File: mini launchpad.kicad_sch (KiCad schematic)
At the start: 75 parts, among them J1 USB_A, P1 USB_C_Plug_USB2.0, U1 MCP23017_ML, U2 MCP23017_ML, U3 MCP23017_ML, U4 MCP23017_ML, U5 CP2615-xx-xM, U6 TMUX1574PW, U7 CH334R

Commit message: pcb update
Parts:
- removed A2: RaspberryPi_Pico, Module:RaspberryPi_Pico_Common_THT, symbol MCU_Module:RaspberryPi_Pico
- removed J1: USB_A, Connector_USB:USB_A_Connfly_DS1095, symbol Connector:USB_A
- added C1, C2: 10µF, Capacitor_SMD:C_0201_0603Metric, symbol Device:C
- added C10, C11, C12, C13, C14, C4, C5, C7, C8, C9: 100nF, Capacitor_SMD:C_0201_0603Metric, symbol Device:C
- added C15, C16: 22pF, Capacitor_SMD:C_0402_1005Metric, symbol Device:C_Small
- added C3, C6: 1µF, Capacitor_SMD:C_0201_0603Metric, symbol Device:C
- added JP1: Jumper_2_Open, Jumper:Jumper_Harwin_S1621_P10.9mm, symbol Jumper:Jumper_2_Open
- added R2, R3: 27, Resistor_SMD:R_0402_1005Metric, symbol Device:R
- added R4: 10K, Resistor_SMD:R_0402_1005Metric, symbol Device:R
- added R5: 1K, Resistor_SMD:R_0402_1005Metric, symbol Device:R
- added R7: 1k, Resistor_SMD:R_0402_1005Metric, symbol Device:R_Small
- added SW65: SW_DPDT_x2, Button_Switch_THT:SW_E-Switch_EG2219_DPDT_Angled, symbol Switch:SW_DPDT_x2
- added U10: W25Q128JVS, Package_SO:SOIC-8_5.3x5.3mm_P1.27mm, symbol Memory_Flash:W25Q128JVS
- added U8: RP2040, Package_DFN_QFN:QFN-56-1EP_7x7mm_P0.4mm_EP3.2x3.2mm, symbol MCU_RaspberryPi:RP2040
- added U9: NCP1117-3.3_TO252, Package_TO_SOT_SMD:TO-252-2, symbol Regulator_Linear:NCP1117-3.3_TO252
- added Y1: 12MHz, Crystal:Crystal_SMD_3225-4Pin_3.2x2.5mm, symbol Device:Crystal_GND24_Small
- R1: value 5100 -> 5.1K
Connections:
- net +3V3: now also C10.2, C11.2, C12.1, C13.1, C14.2, C2.2, C6.1, C7.2, C8.2, C9.2, R4.1, U10.8 (VCC), U8.1 (IOVDD), U8.10 (IOVDD), U8.22 (IOVDD), U8.33 (IOVDD), U8.42 (IOVDD), U8.43 (ADC_AVDD), U8.44 (VREG_IN), U8.48 (USB_VDD), U8.49 (IOVDD), U9.2 (VO)
- net GND: now also C1.1, C10.1, C11.1, C12.2, C13.2, C14.1, C15.1, C16.1, C2.1, C3.2, C4.2, C5.2, C6.2, C7.1, C8.1, C9.1, JP1.2 (B), U10.4 (GND), U8.57 (GND), U9.1 (GND), Y1.2, Y1.4
- net INT1: now also U8.2 (GPIO0)
- net INT2: now also U8.3 (GPIO1)
- net INT3: now also U8.4 (GPIO2)
- net INT4: now also U8.5 (GPIO3)
- net PI_I²S: now also U8.37 (GPIO25)
- net SCK: now also U8.7 (GPIO5)
- net SDA: now also U8.6 (GPIO4)
- net VBUS: now also C1.2, SW65.1 (A), U9.3 (VI); no longer P1.A4 (VBUS), P1.A9 (VBUS), P1.B4 (VBUS), P1.B9 (VBUS)
- net D-1: now reaches U7.7 (DM1-)
- net D-1: now also R3.2
- net D+1: now reaches U7.8 (DP1+)
- net D+1: now also R2.1
- net PI_BLCK: now reaches U6.10 (S3B)
- net PI_BLCK: now also U8.38 (GPIO26_ADC0)
- net PI_LRCLK: now reaches U6.13 (S4B)
- net PI_LRCLK: now also U8.39 (GPIO27_ADC1)
- net PI_DIN: now reaches U6.6 (S2B)
- net PI_DIN: now also U8.40 (GPIO28_ADC2)
- new net: R4.2, R5.1, U10.1 (~{CS}), U8.56 (QSPI_SS)
- new net: U10.2 (DO/IO_{1}), U8.55 (QSPI_SD1)
- new net: U10.3 (~{WP}/IO_{2}), U8.54 (QSPI_SD2)
- new net: U10.5 (DI/IO_{0}), U8.53 (QSPI_SD0)
- new net: U10.6 (CLK), U8.52 (QSPI_SCLK)
- new net: U10.7 (~{HOLD}/~{RESET}/IO_{3}), U8.51 (QSPI_SD3)
- new net: R3.1, U8.46 (USB_DM)
- new net: C15.2, U8.20 (XIN), Y1.3
- new net: R7.2, U8.21 (XOUT)
- new net: R2.2, U8.47 (USB_DP)
- new net: P1.A4 (VBUS), P1.A9 (VBUS), P1.B4 (VBUS), P1.B9 (VBUS), SW65.2 (B)
- new net: JP1.1 (A), R5.2
- new net +1V1: C3.1, C4.1, C5.1, U8.23 (DVDD), U8.45 (VREG_VOUT), U8.50 (DVDD)
- new net XTAL_O: C16.2, R7.1, Y1.1
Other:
- note added: "P43"
- note added: "P45"
- note added: "USB input"
- note added: "USB to I²S and I²S switching"
- note added: "rp2040"
- note added: "voltage regulator"
- moved on the sheet: P1, R1, U5, U6, U7

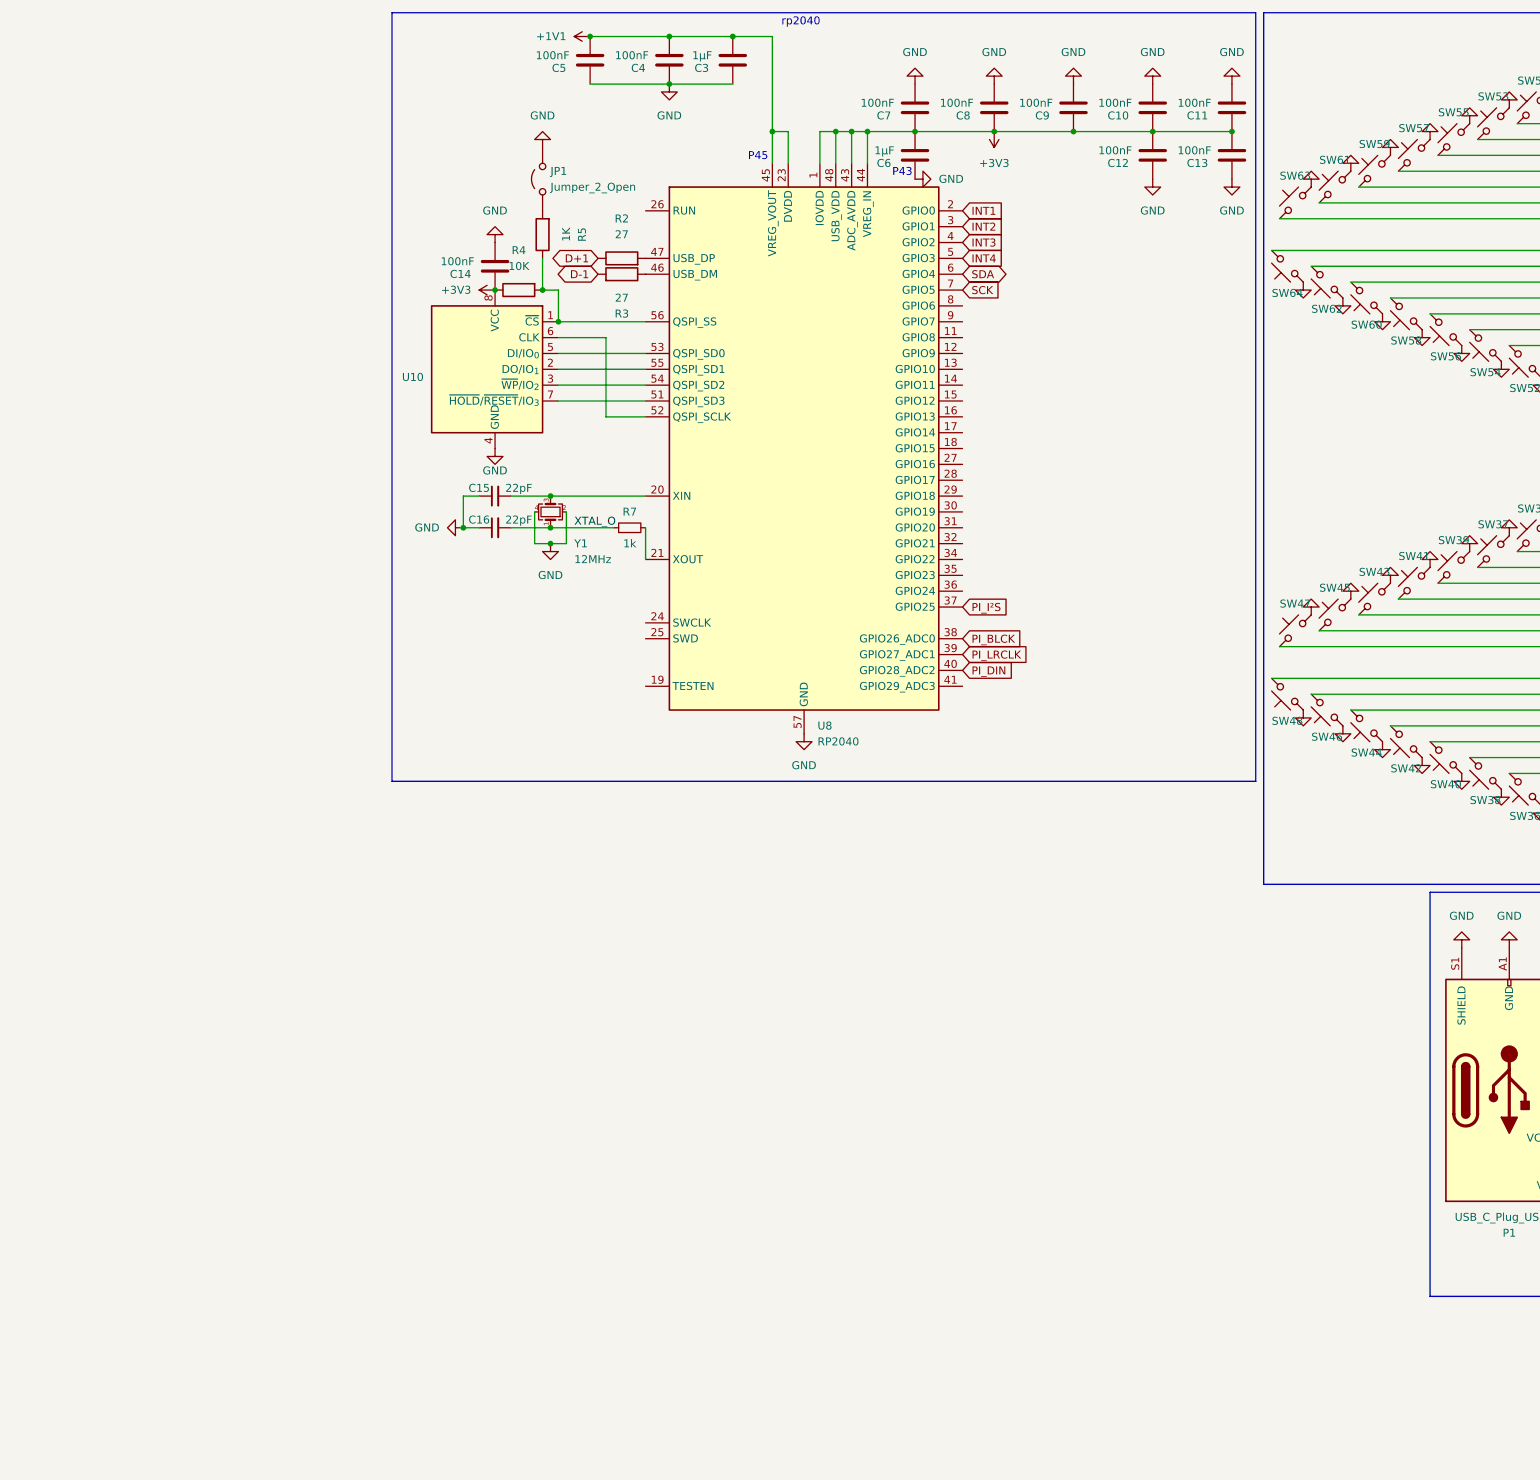
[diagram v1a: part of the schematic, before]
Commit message: schematic update
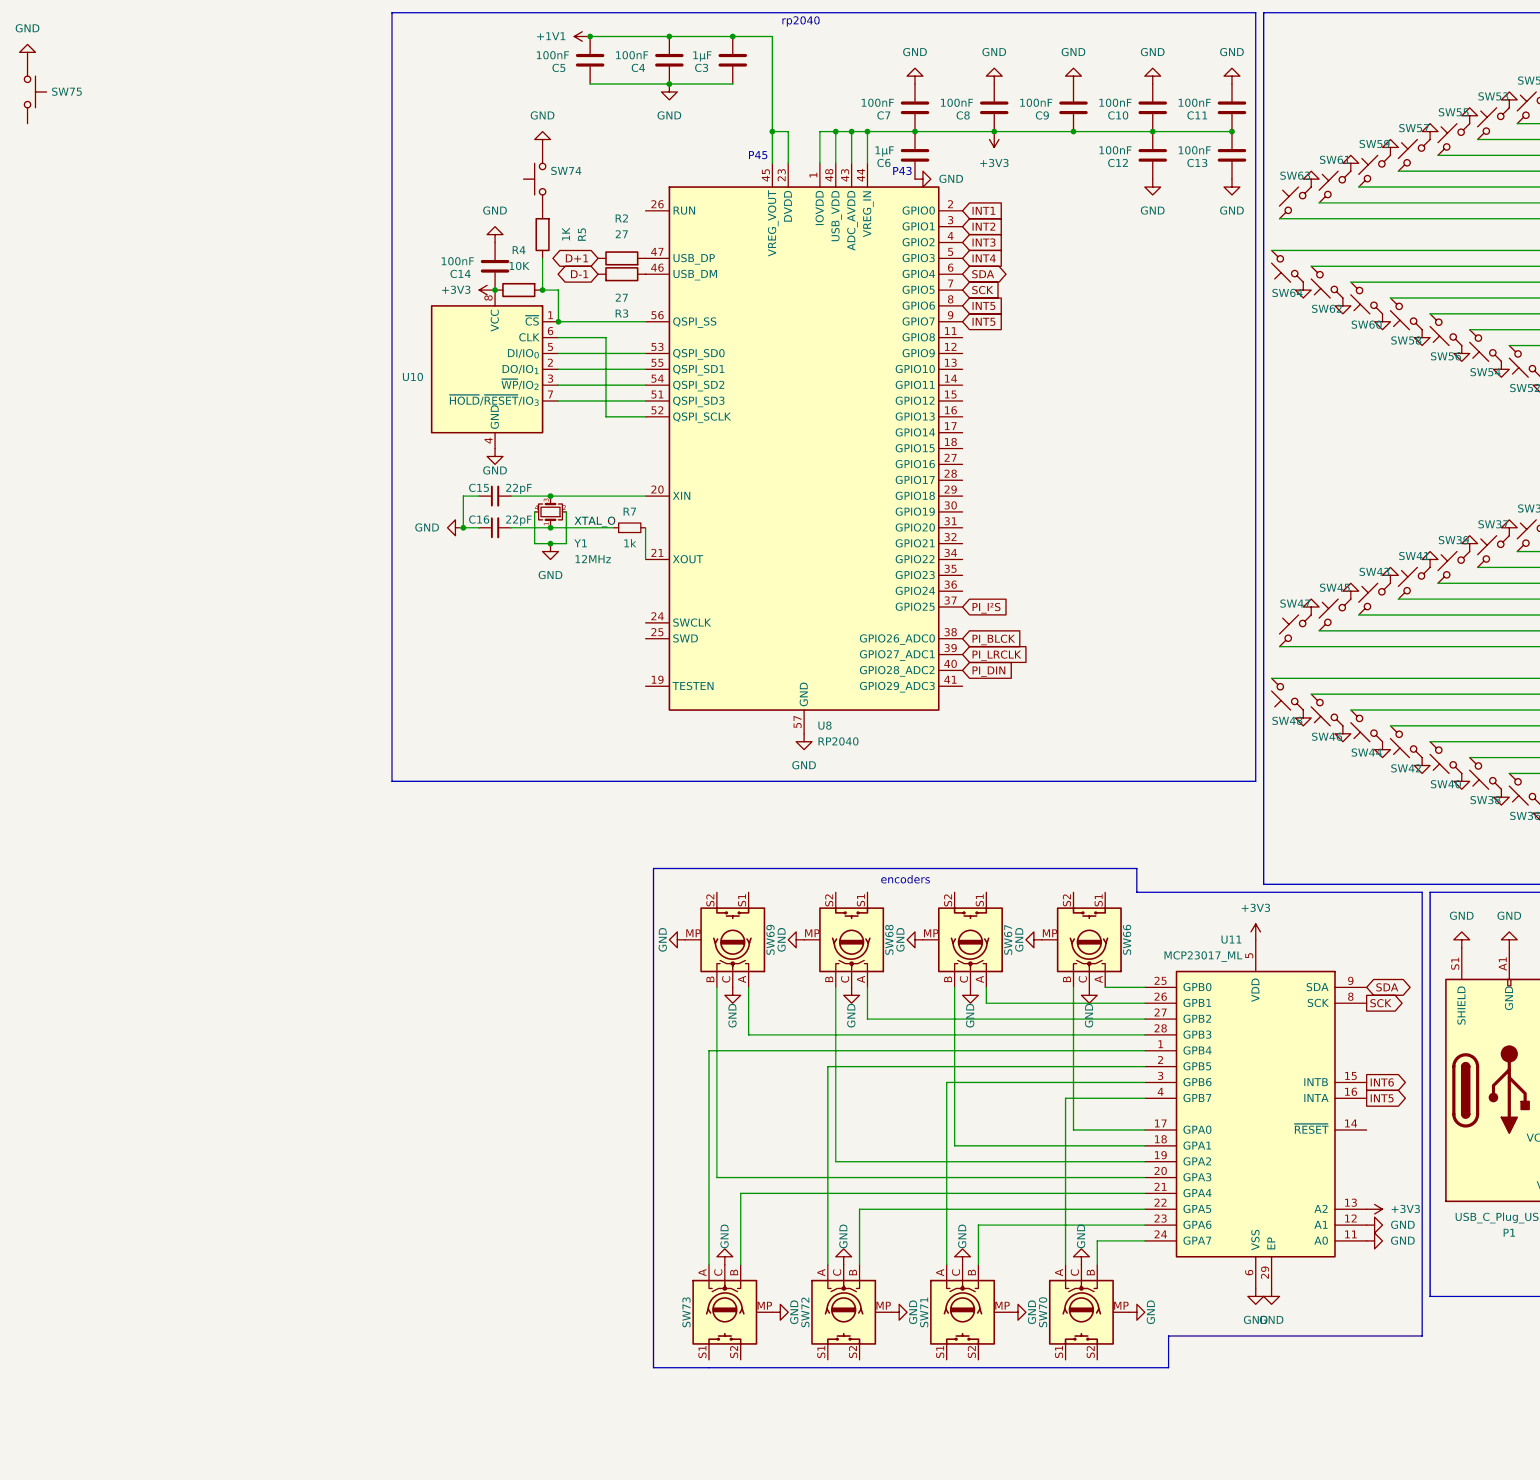
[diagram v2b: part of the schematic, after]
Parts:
- removed JP1: Jumper_2_Open, Jumper:Jumper_Harwin_S1621_P10.9mm, symbol Jumper:Jumper_2_Open
- added SW66, SW67, SW68, SW69, SW70, SW71, SW72, SW73: RotaryEncoder_Switch_MP, Rotary_Encoder:RotaryEncoder_Alps_EC11E-Switch_Vertical_H20mm_MountingHoles, symbol Device:RotaryEncoder_Switch_MP
- added SW74, SW75: SW_Push, symbol Switch:SW_Push
- added U11: MCP23017_ML, Package_DFN_QFN:QFN-28-1EP_6x6mm_P0.65mm_EP4.25x4.25mm, symbol Interface_Expansion:MCP23017_ML
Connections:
- net +3V3: now also U11.13 (A2), U11.5 (VDD)
- net GND: now also SW66.C, SW66.MP, SW67.C, SW67.MP, SW68.C, SW68.MP, SW69.C, SW69.MP, SW70.C, SW70.MP, SW71.C, SW71.MP, SW72.C, SW72.MP, SW73.C, SW73.MP, SW74.2, SW75.1, U11.11 (A0), U11.12 (A1), U11.29 (EP), U11.6 (VSS)
- net SCK: now also U11.8 (SCK)
- net SDA: now also U11.9 (SDA)
- net INT5: now reaches U8.8 (GPIO6)
- net INT5: now also U8.9 (GPIO7), U11.16 (INTA)
- net at R5.2: now also SW74.1
- new net: SW69.A, U11.28 (GPB3)
- new net: SW69.B, U11.20 (GPA3)
- new net: SW70.A, U11.4 (GPB7)
- new net: SW70.B, U11.24 (GPA7)
- new net: SW73.A, U11.1 (GPB4)
- new net: SW73.B, U11.21 (GPA4)
- new net: SW71.A, U11.3 (GPB6)
- new net: SW71.B, U11.23 (GPA6)
- new net: SW68.A, U11.27 (GPB2)
- new net: SW68.B, U11.19 (GPA2)
- new net: SW66.B, U11.17 (GPA0)
- new net: SW67.B, U11.18 (GPA1)
- new net: SW72.A, U11.2 (GPB5)
- new net: SW72.B, U11.22 (GPA5)
- new net: SW66.A, U11.25 (GPB0)
- new net: SW67.A, U11.26 (GPB1)
- new net INT6: U11.15 (INTB)
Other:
- note added: "encoders"

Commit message: pcb update
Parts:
- added D1, D2: LED, LED_SMD:LED_1206_3216Metric, symbol Device:LED
- added D3: GREEN_LED, LED_SMD:LED_1206_3216Metric, symbol Device:LED
- added R6, R8, R9: 220, Resistor_SMD:R_0402_1005Metric, symbol Device:R
- added SW76, SW77, SW78, SW79, SW80, SW81, SW82: SW_Push, Button_Switch_Keyboard:SW_Cherry_MX_1.00u_PCB, symbol Switch:SW_Push
- added SW84: RotaryEncoder_Switch_MP, Rotary_Encoder:RotaryEncoder_Alps_EC11E-Switch_Vertical_H20mm_MountingHoles, symbol Device:RotaryEncoder_Switch_MP
- SW74, SW75: footprint (none) -> Button_Switch_Keyboard:SW_Cherry_MX_1.00u_PCB
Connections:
- net GND: now also D1.1 (K), D2.1 (K), D3.1 (K), SW76.1, SW77.1, SW78.1, SW79.1, SW80.1, SW81.1, SW82.1, SW84.C, SW84.MP
- new net: D2.2 (A), R8.2
- new net: D1.2 (A), R6.2
- new net: D3.2 (A), R9.2

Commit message: pcb update
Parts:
- removed SW82: SW_Push, Button_Switch_Keyboard:SW_Cherry_MX_1.00u_PCB, symbol Switch:SW_Push
- removed SW84: RotaryEncoder_Switch_MP, Rotary_Encoder:RotaryEncoder_Alps_EC11E-Switch_Vertical_H20mm_MountingHoles, symbol Device:RotaryEncoder_Switch_MP
- added C17, C18, C21, C22: 10µF, Capacitor_SMD:C_0201_0603Metric, symbol Device:C
- added C19, C24: 250µF, Capacitor_SMD:C_0201_0603Metric, symbol Device:C
- added C20, C23: 0.05µF, Capacitor_SMD:C_0201_0603Metric, symbol Device:C
- added R10, R13: 10, Resistor_SMD:R_0402_1005Metric, symbol Device:R
- added R11, R12: 10K, Resistor_SMD:R_0402_1005Metric, symbol Device:R
- added R14, R15: 100, Resistor_SMD:R_0402_1005Metric, symbol Device:R
- added RV2: R_Potentiometer_Dual, Potentiometer_THT:Potentiometer_Alpha_RD902F-40-00D_Dual_Vertical, symbol Device:R_Potentiometer_Dual
- added SW83: SW_Push, Button_Switch_Keyboard:SW_Cherry_MX_1.00u_PCB, symbol Switch:SW_Push
- added U12, U13: LM386, Package_DIP:DIP-8_W7.62mm_Socket, symbol Amplifier_Audio:LM386
- D3: value GREEN_LED -> LED
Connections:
- net GND: now also C18.1, C22.1, R10.2, R11.1, R12.1, R13.2, SW83.1, U12.2 (-), U12.4 (GND), U13.2 (-), U13.4 (GND)
- net VBUS: now also U12.6 (V+), U13.6 (V+)
- net GPIO20: now reaches SW79.2
- net GPIO20: now also U8.31 (GPIO20)
- net GPIO16: now reaches R6.1
- net GPIO16: now also U8.27 (GPIO16)
- net GPIO18: now reaches SW80.2
- net GPIO18: now also U8.29 (GPIO18)
- net GPIO14: now reaches R9.1
- net GPIO14: now also U8.17 (GPIO14)
- net GPIO24: now reaches SW75.2
- net GPIO24: now also U8.36 (GPIO24)
- net GPIO21: now reaches SW78.2
- net GPIO21: now also U8.32 (GPIO21)
- net GPIO15: now reaches U8.18 (GPIO15)
- net GPIO15: now also R8.1
- net GPIO17: now reaches U8.28 (GPIO17)
- net GPIO17: now also SW81.2
- net GPIO19: now reaches U8.30 (GPIO19)
- net GPIO19: now also SW83.2
- net GPIO22: now reaches U8.34 (GPIO22)
- net GPIO22: now also SW77.2
- net GPIO23: now reaches U8.35 (GPIO23)
- net GPIO23: now also SW76.2
- new net: C17.1, U12.1 (GAIN)
- new net: C19.1, C20.1, U12.5
- new net: C18.2, U12.7 (BYPASS)
- new net: RV2.2, U12.8 (GAIN)
- new net: C22.2, U13.7 (BYPASS)
- new net: C23.1, C24.1, U13.5
- new net: C24.2, R15.2
- new net: C23.2, R13.1
- new net: C19.2, R14.2
- new net: C20.2, R10.1
- new net: C17.2, RV2.1
- new net: C21.1, U13.1 (GAIN)
- new net: RV2.5, U13.8 (GAIN)
- new net: C21.2, RV2.4
- new net lineL: R11.2, U12.3 (+)
- new net lineR: R12.2, U13.3 (+)
- new net outL: R14.1
- new net outR: R15.1
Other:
- note added: "amp"
- note added: "control"
- moved on the sheet: D1, D2, D3, R6, R8, R9, SW80, SW81

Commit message: pcb update
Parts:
- added J1: Conn_01x08_Socket, Connector_PinHeader_2.54mm:PinHeader_1x08_P2.54mm_Vertical, symbol Connector:Conn_01x08_Socket
- added J2: Conn_01x06_Socket, Connector_PinHeader_2.54mm:PinHeader_1x06_P2.54mm_Vertical, symbol Connector:Conn_01x06_Socket
- added Q1: AO3401A, Package_TO_SOT_SMD:SOT-23, symbol Transistor_FET:AO3401A
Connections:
- net +3V3: now also Q1.3 (D)
- net GND: now also J1.2 (Pin_2), J1.7 (Pin_7)
- net lineL: now also J1.6 (Pin_6)
- net lineR: now also J1.8 (Pin_8)
- net GPIO13: now reaches U8.16 (GPIO13)
- net GPIO13: now also Q1.1 (G)
- net LRCLK: now reaches U6.12 (D4)
- net LRCLK: now also J1.3 (Pin_3)
- net DIN: now reaches U6.7 (D2)
- net DIN: now also J1.4 (Pin_4)
- net BLCK: now reaches U6.9 (D3)
- net BLCK: now also J1.5 (Pin_5)
- new net: J1.1 (Pin_1), Q1.2 (S)
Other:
- note added: "DAC"

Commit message: pcb update
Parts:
- U7: footprint Connector_USB:USB_C_Plug_Molex_105444 -> Package_SO:QSOP-16_3.9x4.9mm_P0.635mm
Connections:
- net at SW47.2: now also U3.18 (GPA1); no longer U3.4 (GPB7)
- net at SW40.2: now also U3.4 (GPB7); no longer U3.21 (GPA4)
- net at SW23.2: now also U2.3 (GPB6); no longer U2.28 (GPB3)
- net at SW62.2: now also U4.19 (GPA2); no longer U4.18 (GPA1)
- net at U3.1 (GPB4): now also SW37.2; no longer SW41.2
- net at SW46.2: now also U3.19 (GPA2); no longer U3.18 (GPA1)
- net at SW44.2: now also U3.21 (GPA4); no longer U3.19 (GPA2)
- net at U3.2 (GPB5): now also SW38.2; no longer SW43.2
- net at U3.20 (GPA3): now also SW45.2; no longer SW42.2
- net at U3.22 (GPA5): now also SW43.2; no longer SW38.2
- net at U3.23 (GPA6): now also SW42.2; no longer SW36.2
- net at U3.24 (GPA7): now also SW41.2; no longer SW34.2
- net at U3.26 (GPB1): now also SW34.2; no longer SW35.2
- net at U3.27 (GPB2): now also SW35.2; no longer SW37.2
- net at U3.28 (GPB3): now also SW36.2; no longer SW39.2
- net at U3.3 (GPB6): now also SW39.2; no longer SW45.2
- net at SW69.A: now also U11.1 (GPB4); no longer U11.28 (GPB3)
- net at SW69.B: now also U11.21 (GPA4); no longer U11.20 (GPA3)
- net D-: now reaches P1.A7 (D-), U7.10 (DMU-)
- net D+: now reaches P1.A6 (D+), U7.11 (DPU+)
- net at SW29.2: now also U2.20 (GPA3); no longer U2.3 (GPB6)
- net at SW18.2: now also U2.26 (GPB1); no longer U2.24 (GPA7)
- net at SW52.2: now also U4.28 (GPB3); no longer U4.23 (GPA6)
- net at SW55.2: now also U4.3 (GPB6); no longer U4.28 (GPB3)
- net at SW22.2: now also U2.2 (GPB5); no longer U2.22 (GPA5)
- net at U2.1 (GPB4): now also SW21.2; no longer SW25.2
- net at U2.18 (GPA1): now also SW31.2; no longer SW30.2
- net at U2.19 (GPA2): now also SW30.2; no longer SW28.2
- net at SW27.2: now also U2.22 (GPA5); no longer U2.2 (GPB5)
- net at SW26.2: now also U2.23 (GPA6); no longer U2.20 (GPA3)
- net at U2.21 (GPA4): now also SW28.2; no longer SW24.2
- net at SW20.2: now also U2.28 (GPB3); no longer U2.23 (GPA6)
- net at SW19.2: now also U2.27 (GPB2); no longer U2.26 (GPB1)
- net at U2.4 (GPB7): now also SW24.2; no longer SW31.2
- net at SW60.2: now also U4.21 (GPA4); no longer U4.19 (GPA2)
- net at SW70.A: now also U11.28 (GPB3); no longer U11.4 (GPB7)
- net at SW70.B: now also U11.20 (GPA3); no longer U11.24 (GPA7)
- net at U4.1 (GPB4): now also SW53.2; no longer SW57.2
- net at U4.2 (GPB5): now also SW54.2; no longer SW59.2
- net at U4.20 (GPA3): now also SW61.2; no longer SW58.2
- net at SW56.2: now also U4.4 (GPB7); no longer U4.21 (GPA4)
- net at U4.22 (GPA5): now also SW59.2; no longer SW54.2
- net at U4.24 (GPA7): now also SW57.2; no longer SW50.2
- net at U4.26 (GPB1): now also SW50.2; no longer SW51.2
- net at U4.27 (GPB2): now also SW51.2; no longer SW53.2
- net at SW63.2: now also U4.18 (GPA1); no longer U4.4 (GPB7)
- net at SW73.A: now also U11.25 (GPB0); no longer U11.1 (GPB4)
- net at SW73.B: now also U11.17 (GPA0); no longer U11.21 (GPA4)
- net at SW71.A: now also U11.27 (GPB2); no longer U11.3 (GPB6)
- net at SW71.B: now also U11.19 (GPA2); no longer U11.23 (GPA6)
- net at SW68.A: now also U11.2 (GPB5); no longer U11.27 (GPB2)
- net at SW68.B: now also U11.22 (GPA5); no longer U11.19 (GPA2)
- net at SW66.B: now also U11.24 (GPA7); no longer U11.17 (GPA0)
- net at U11.18 (GPA1): now also SW72.B; no longer SW67.B
- net at SW72.A: now also U11.26 (GPB1); no longer U11.2 (GPB5)
- net at SW66.A: now also U11.4 (GPB7); no longer U11.25 (GPB0)
- net at SW67.A: now also U11.3 (GPB6); no longer U11.26 (GPB1)
- net D+1 renamed 1D+
- net D+2 renamed 2D+
- net D-1 renamed 1D-
- net D-2 renamed 2D-
- new net: SW25.2, U2.24 (GPA7)
- new net: SW58.2, U4.23 (GPA6)
- new net: SW67.B, U11.23 (GPA6)
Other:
- moved on the sheet: SW18, SW19, SW20, SW21, SW22, SW23, SW24, SW25, SW26, SW27, SW28, SW29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
